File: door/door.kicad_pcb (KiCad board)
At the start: 2 copper layers, 26.2 x 21 mm, 11 parts, among them J1 POWER, J2 CONTROL, J3 ENDPOINT, J4 MOTOR, Q1 IRF3205

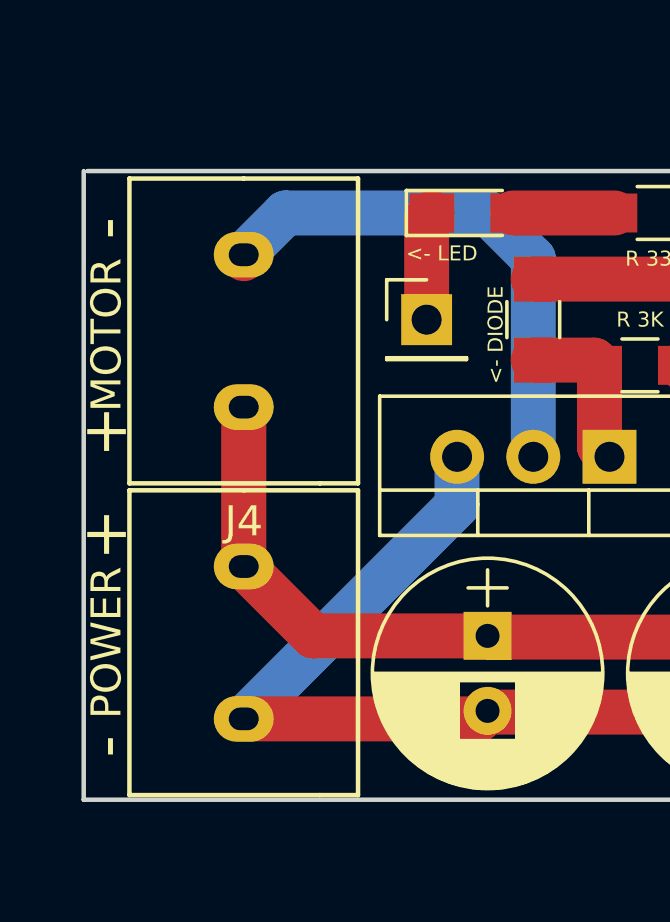
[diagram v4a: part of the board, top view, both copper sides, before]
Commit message: Fixed text-based issues and updated screw terminal footprint
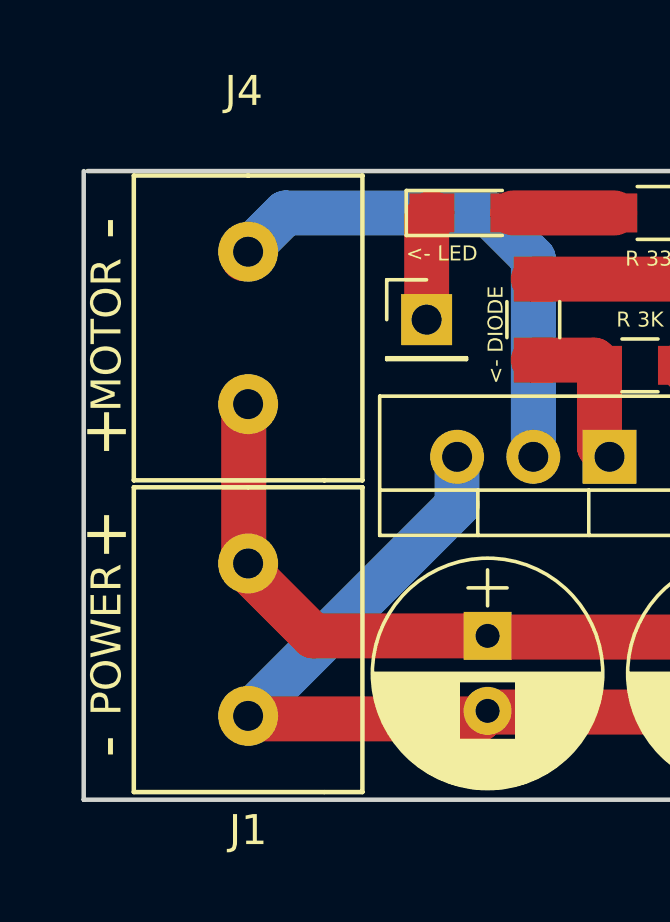
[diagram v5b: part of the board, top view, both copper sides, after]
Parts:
- moved J1 0.18 mm to (133.8, 113.8)
- moved J4 0.18 mm to (133.8, 103.4)
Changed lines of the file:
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@@
     (links 16)
     (no_connects 0)
-    (area 128.194999 98.095999 154.507001 119.201001)
+    (area 127.832 94.327809 158.555 121.57219)
     (thickness 1.6)
     (drawings 13)
@@
   )
   (module library:screw-terminal-01x02 (layer F.Cu)
-    (at 133.604 113.892)
-    (fp_text reference J1 (at 0 6.35) (layer F.CrtYd)
-      (effects (font (size 1 1) (thickness 0.15)))
-    )
-    (fp_text value POWER (at -4.572 0 90) (layer F.SilkS)
+    (at 133.75 113.792)
+    (fp_text reference J1 (at 0 6.35) (layer F.SilkS)
+      (effects (font (size 1 1) (thickness 0.15)))
+    )
+    (fp_text value POWER (at -4.718 0 90) (layer F.SilkS)
       (effects (font (size 1 1) (thickness 0.15)))
     )
@@
     (fp_line (start 3.81 5.08) (end 3.81 -5.08) (layer F.SilkS) (width 0.15))
     (fp_line (start 3.81 -5.08) (end 0 -5.08) (layer F.SilkS) (width 0.15))
-    (pad 1 thru_hole oval (at 0 -2.54) (size 2 1.524) (drill oval 1 0.762) (layers *.Cu *.Mask)
+    (pad 1 thru_hole circle (at 0 -2.54) (size 2 2) (drill 1) (layers *.Cu *.Mask)
       (net 2 +12V))
-    (pad 2 thru_hole oval (at 0 2.54) (size 2 1.524) (drill oval 1 0.762) (layers *.Cu *.Mask)
+    (pad 2 thru_hole circle (at 0 2.54) (size 2 2) (drill 1) (layers *.Cu *.Mask)
       (net 1 GND))
   )
   (module library:screw-terminal-01x02 (layer F.Cu)
-    (at 133.604 103.5)
-    (fp_text reference J4 (at 0 6.35) (layer F.SilkS)
-      (effects (font (size 1 1) (thickness 0.15)))
-    )
-    (fp_text value MOTOR (at -4.572 0.132 90) (layer F.SilkS)
+    (at 133.75 103.4)
+    (fp_text reference J4 (at -0.146 -7.896) (layer F.SilkS)
+      (effects (font (size 1 1) (thickness 0.15)))
+    )
+    (fp_text value MOTOR (at -4.718 0.232 90) (layer F.SilkS)
       (effects (font (size 1 1) (thickness 0.15)))
     )
@@
     (fp_line (start 3.81 5.08) (end 3.81 -5.08) (layer F.SilkS) (width 0.15))
     (fp_line (start 3.81 -5.08) (end 0 -5.08) (layer F.SilkS) (width 0.15))
-    (pad 1 thru_hole oval (at 0 -2.54) (size 2 1.524) (drill oval 1 0.762) (layers *.Cu *.Mask)
+    (pad 1 thru_hole circle (at 0 -2.54) (size 2 2) (drill 1) (layers *.Cu *.Mask)
       (net 6 "Net-(J4-Pad1)"))
-    (pad 2 thru_hole oval (at 0 2.54) (size 2 1.524) (drill oval 1 0.762) (layers *.Cu *.Mask)
+    (pad 2 thru_hole circle (at 0 2.54) (size 2 2) (drill 1) (layers *.Cu *.Mask)
       (net 2 +12V))
   )
@@
     (effects (font (size 1.5 1.5) (thickness 0.3)))
   )
-  (segment (start 150.241 116.165) (end 152.567 116.165) (width 1.5) (layer F.Cu) (net 1) (status 400000))
-  (segment (start 152.908 115.824) (end 152.908 109.22) (width 1.5) (layer F.Cu) (net 1) (status 800000))
+  (segment (start 150.241 116.165) (end 152.567 116.165) (width 1.5) (layer F.Cu) (net 1))
+  (segment (start 152.908 115.824) (end 152.908 109.22) (width 1.5) (layer F.Cu) (net 1))
   (segment (start 152.567 116.165) (end 152.908 115.824) (width 1.5) (layer F.Cu) (net 1))
-  (segment (start 152.908 109.22) (end 152.4 108.712) (width 1.5) (layer F.Cu) (net 1) (status C00000))
-  (segment (start 140.716 107.696) (end 140.716 109.32) (width 1.5) (layer B.Cu) (net 1) (status 400000))
-  (segment (start 140.716 109.32) (end 133.604 116.432) (width 1.5) (layer B.Cu) (net 1) (status 800000))
-  (segment (start 152.4 108.712) (end 152.4 106.172) (width 1.5) (layer F.Cu) (net 1) (status C00000))
-  (segment (start 152.4 106.172) (end 149.686 106.172) (width 1.5) (layer F.Cu) (net 1) (status 400000))
-  (segment (start 149.686 106.172) (end 148.162 104.648) (width 1.5) (layer F.Cu) (net 1) (status 800000))
+  (segment (start 152.908 109.22) (end 152.4 108.712) (width 1.5) (layer F.Cu) (net 1))
+  (segment (start 140.716 107.696) (end 140.716 109.32) (width 1.5) (layer B.Cu) (net 1))
+  (segment (start 140.716 109.32) (end 133.604 116.432) (width 1.5) (layer B.Cu) (net 1))
+  (segment (start 152.4 108.712) (end 152.4 106.172) (width 1.5) (layer F.Cu) (net 1))
+  (segment (start 152.4 106.172) (end 149.686 106.172) (width 1.5) (layer F.Cu) (net 1))
+  (segment (start 149.686 106.172) (end 148.162 104.648) (width 1.5) (layer F.Cu) (net 1))
   (segment (start 133.604 116.432) (end 141.465 116.432) (width 1.5) (layer F.Cu) (net 1))
   (segment (start 141.465 116.432) (end 141.732 116.165) (width 1.5) (layer F.Cu) (net 1))
@@
   (segment (start 135.917 113.665) (end 133.604 111.352) (width 1.5) (layer F.Cu) (net 2))
   (segment (start 141.732 113.705) (end 150.241 113.705) (width 1.5) (layer F.Cu) (net 2))
-  (segment (start 139.7 103.124) (end 139.7 99.742) (width 1.5) (layer F.Cu) (net 3) (status C00000))
-  (segment (start 139.7 99.742) (end 139.874 99.568) (width 1.5) (layer F.Cu) (net 3) (status C00000))
-  (segment (start 142.574 99.568) (end 145.97 99.568) (width 1.5) (layer F.Cu) (net 4) (status C00000))
-  (segment (start 148.67 99.568) (end 150.876 99.568) (width 1.5) (layer F.Cu) (net 5) (status 400000))
-  (segment (start 150.876 99.568) (end 152.4 101.092) (width 1.5) (layer F.Cu) (net 5) (status 800000))
-  (segment (start 143.256 107.696) (end 143.256 101.092) (width 1.5) (layer B.Cu) (net 6) (status 400000))
-  (segment (start 134.996 99.568) (end 133.604 100.96) (width 1.5) (layer B.Cu) (net 6) (status 800000))
+  (segment (start 139.7 103.124) (end 139.7 99.742) (width 1.5) (layer F.Cu) (net 3))
+  (segment (start 139.7 99.742) (end 139.874 99.568) (width 1.5) (layer F.Cu) (net 3))
+  (segment (start 142.574 99.568) (end 145.97 99.568) (width 1.5) (layer F.Cu) (net 4))
+  (segment (start 148.67 99.568) (end 150.876 99.568) (width 1.5) (layer F.Cu) (net 5))
+  (segment (start 150.876 99.568) (end 152.4 101.092) (width 1.5) (layer F.Cu) (net 5))
+  (segment (start 133.604 100.96) (end 133.604 101.092) (width 1.5) (layer F.Cu) (net 6))
+  (segment (start 143.256 107.696) (end 143.256 101.092) (width 1.5) (layer B.Cu) (net 6))
+  (segment (start 134.996 99.568) (end 133.604 100.96) (width 1.5) (layer B.Cu) (net 6))
   (segment (start 141.732 99.568) (end 134.996 99.568) (width 1.5) (layer B.Cu) (net 6))
   (segment (start 143.256 101.092) (end 141.732 99.568) (width 1.5) (layer B.Cu) (net 6))
-  (segment (start 133.604 100.96) (end 133.604 101.092) (width 1.5) (layer F.Cu) (net 6) (status C00000))
-  (segment (start 145.462 104.648) (end 145.462 107.362) (width 1.5) (layer F.Cu) (net 7) (status C00000))
-  (segment (start 145.462 107.362) (end 145.796 107.696) (width 1.5) (layer F.Cu) (net 7) (status C00000))
-  (segment (start 143.256 104.474) (end 145.288 104.474) (width 1.5) (layer F.Cu) (net 7) (status C00000))
-  (segment (start 145.288 104.474) (end 145.462 104.648) (width 1.5) (layer F.Cu) (net 7) (status C00000))
-  (segment (start 152.4 103.632) (end 151.384 103.632) (width 1.5) (layer F.Cu) (net 8) (status 400000))
-  (segment (start 149.526 101.774) (end 143.256 101.774) (width 1.5) (layer F.Cu) (net 8) (status 800000))
+  (segment (start 145.462 104.648) (end 145.462 107.362) (width 1.5) (layer F.Cu) (net 7))
+  (segment (start 145.462 107.362) (end 145.796 107.696) (width 1.5) (layer F.Cu) (net 7))
+  (segment (start 143.256 104.474) (end 145.288 104.474) (width 1.5) (layer F.Cu) (net 7))
+  (segment (start 145.288 104.474) (end 145.462 104.648) (width 1.5) (layer F.Cu) (net 7))
+  (segment (start 152.4 103.632) (end 151.384 103.632) (width 1.5) (layer F.Cu) (net 8))
+  (segment (start 149.526 101.774) (end 143.256 101.774) (width 1.5) (layer F.Cu) (net 8))
   (segment (start 151.384 103.632) (end 149.526 101.774) (width 1.5) (layer F.Cu) (net 8))
 )
